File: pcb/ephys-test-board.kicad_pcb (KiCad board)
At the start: 4 copper layers, 150 x 120 mm, 567 parts, among them J1 10129383-910002ALF, J2 BM03B-SRSS-TB, J3 BTE-040-03-L-D-A, J4 BTE-040-03-L-D-A, J5 731000105, J6 USB4105-GF-A, J7 S2B-PH-SM4-TB, J8 FH12-16S-0.5SH(55), Q1 DMP3099L-7, Q2 DMG3418L-7, Q3 DMG3418L-7, Q4 DMG3418L-7, Q5 DMP3099L-7, SW1 PTS645VH83-2 LFS, SW2 TS04-66-50-BK-160-SMT, SW3 400MSP1R6BLKM6QE, SW4 PEC12R-4220F-S0024, U1 W25Q128JVSIQ, U10 FSA553UCX, U11 FSA553UCX, U12 SN74HC595PWR, U13 FSA553UCX, U14 FSA553UCX, U15 FSA553UCX, U16 FSA553UCX, U17 SN74HC595PWR, U18 FSA553UCX, U19 FSA553UCX, U2 SC0914(13), U20 FSA553UCX, U21 FSA553UCX, U22 SN74HC595PWR, U23 FSA553UCX, U24 FSA553UCX, U25 FSA553UCX, U26 FSA553UCX, U27 SN74HC595PWR, U28 FSA553UCX, U29 FSA553UCX, U3 FSA553UCX, U30 FSA553UCX, U31 FSA553UCX, U32 SN74HC595PWR, U33 FSA553UCX, U34 FSA553UCX, U35 FSA553UCX, U36 FSA553UCX, U37 SN74HC595PWR, U38 FSA553UCX, U39 FSA553UCX, U4 FSA553UCX, U40 FSA553UCX, U41 FSA553UCX, U42 SN74HC595PWR, U43 FSA553UCX, U44 FSA553UCX, U45 FSA553UCX, U46 FSA553UCX, U47 SN74HC595PWR, U48 FSA553UCX, U49 FSA553UCX, U5 FSA553UCX, U50 FSA553UCX, U51 FSA553UCX, U52 SN74HC595PWR, U53 FSA553UCX, U54 FSA553UCX, U55 FSA553UCX, U56 FSA553UCX, U57 SN74HC595PWR, U58 FSA553UCX, U59 FSA553UCX, U6 FSA553UCX, U60 FSA553UCX, U61 FSA553UCX, U62 SN74HC595PWR, U63 FSA553UCX, U64 FSA553UCX, U65 FSA553UCX, U66 FSA553UCX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

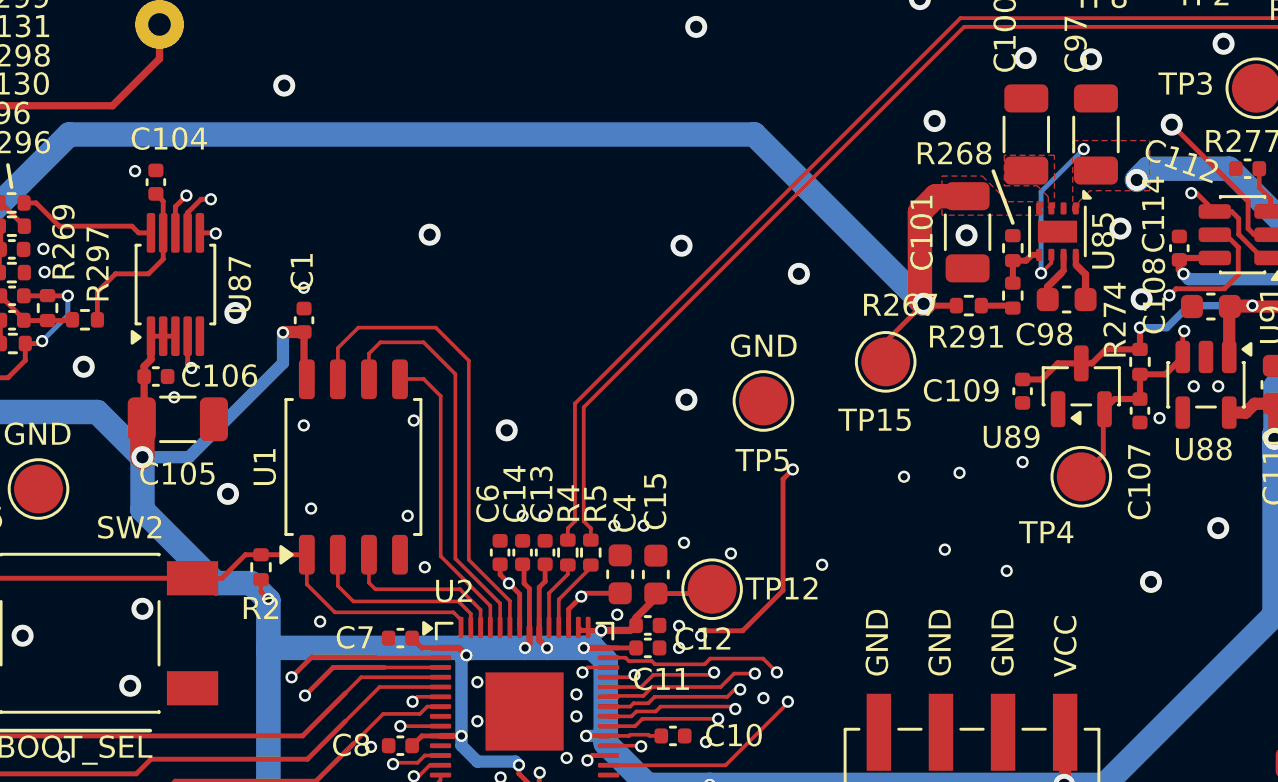
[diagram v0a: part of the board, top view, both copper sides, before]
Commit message: Rev. G candidate
- Upgrade to KiCad 10
- Fix schematic comments
- Move html bom to pcb directory
- No changes in parts, no changes in part positions. Small internal
  routing changes for the switched cap inverter
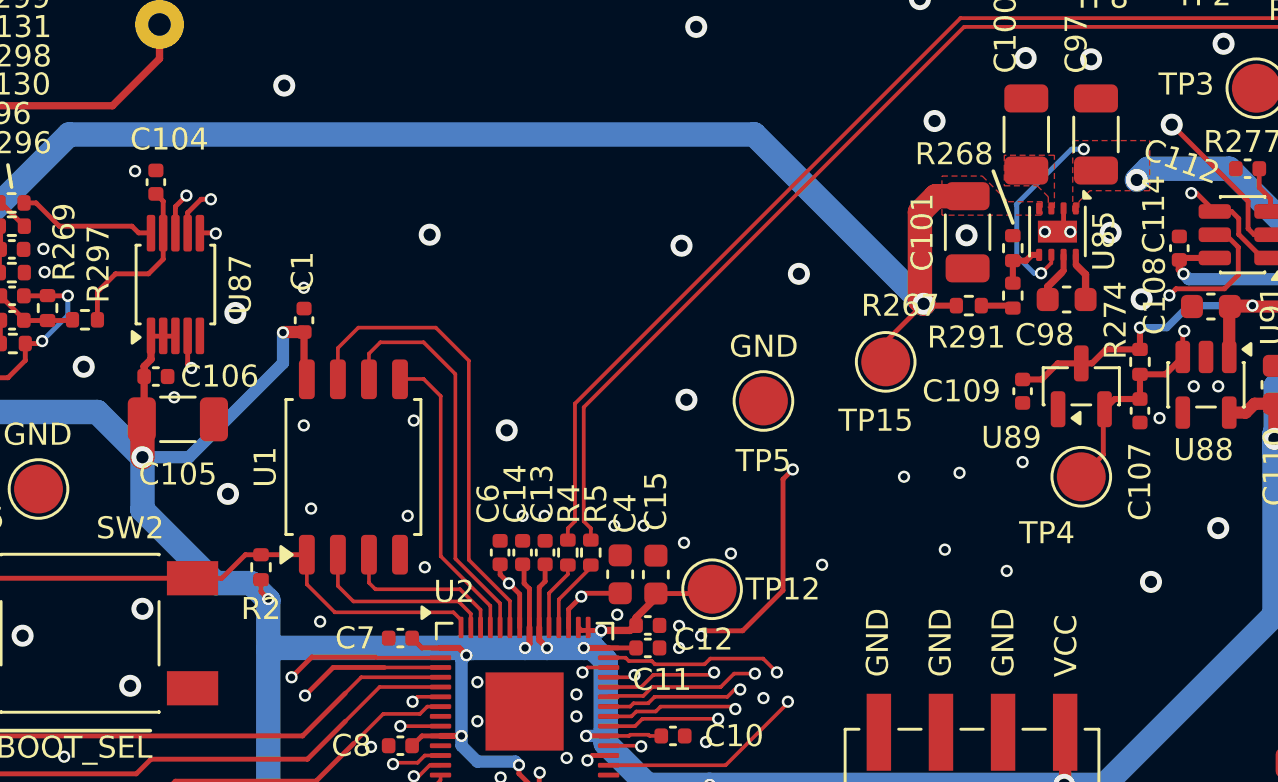
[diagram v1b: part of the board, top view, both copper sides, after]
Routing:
- net /MCU/VBus_{Detect}: track 59.2 -> 66.2 mm
- net VCC: track 965.0 -> 966.3 mm
- net GND: track 225.8 -> 226.8 mm, vias 523 -> 525
